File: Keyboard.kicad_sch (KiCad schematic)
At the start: 39 parts, among them J1 USB_C_Receptacle, J2 Conn_02x01, J4 FFC2B35-16-G_REVA2, Q1 PMOS, Q2 NMOS, Q3 NMOS, U1 VBUS54CV-HSF-G4-08, U3 MCP73831-2-OT, U4 LM1117DT-3.3, U5 ESP32-S3-WROOM-1-N16R2

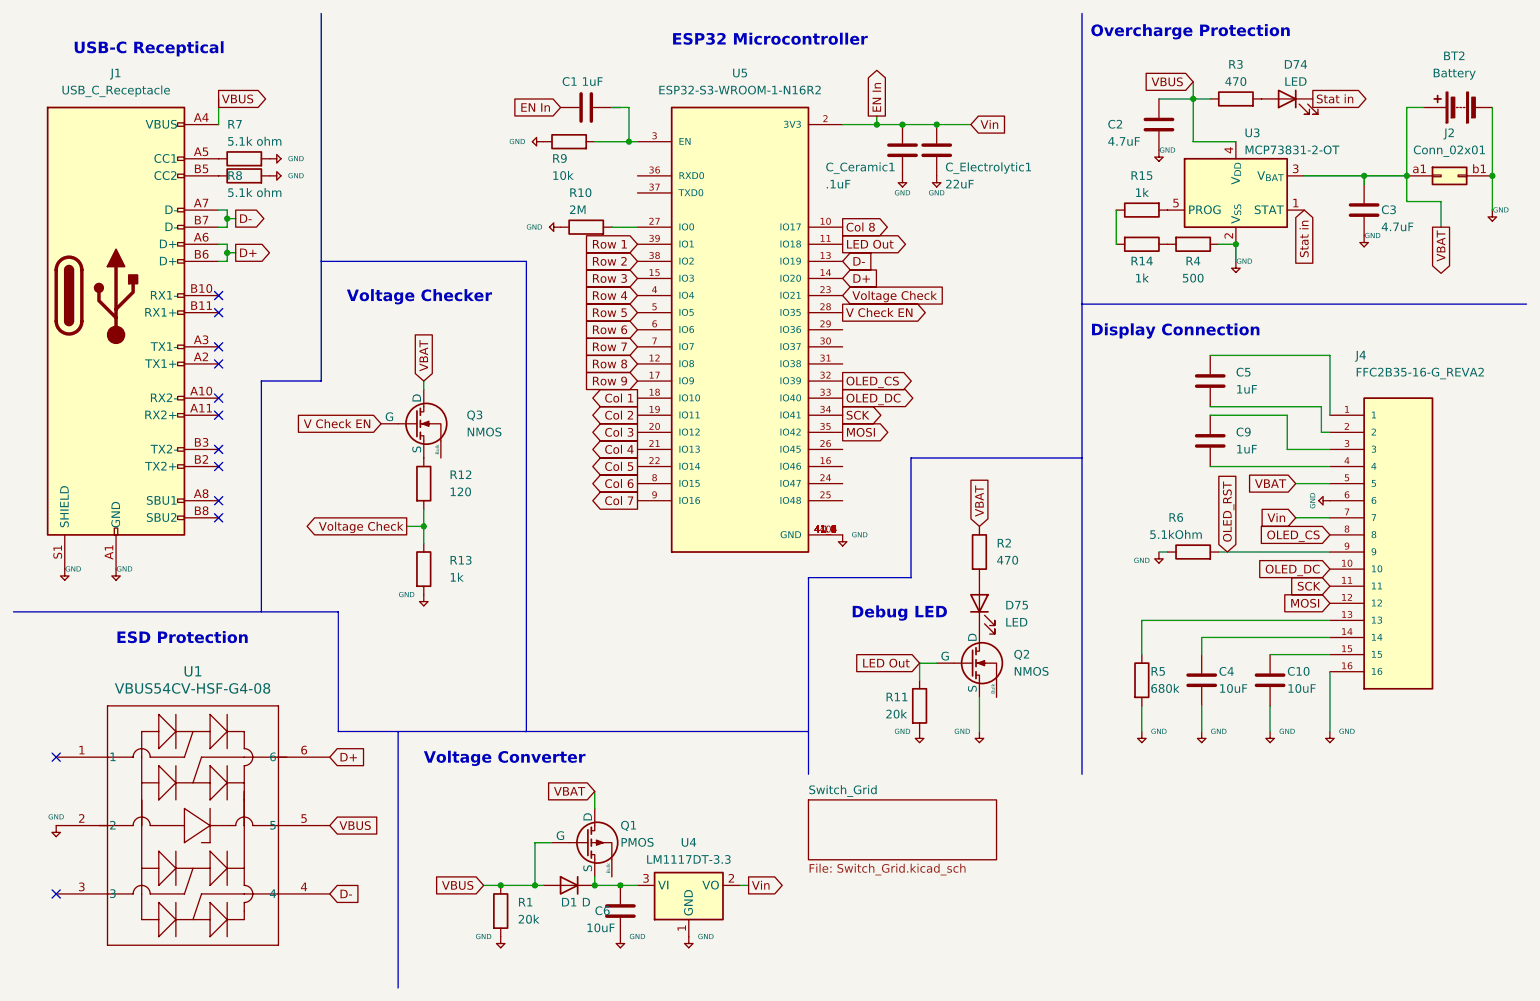
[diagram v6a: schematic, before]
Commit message: finished logic layout, need to connect pins to keys
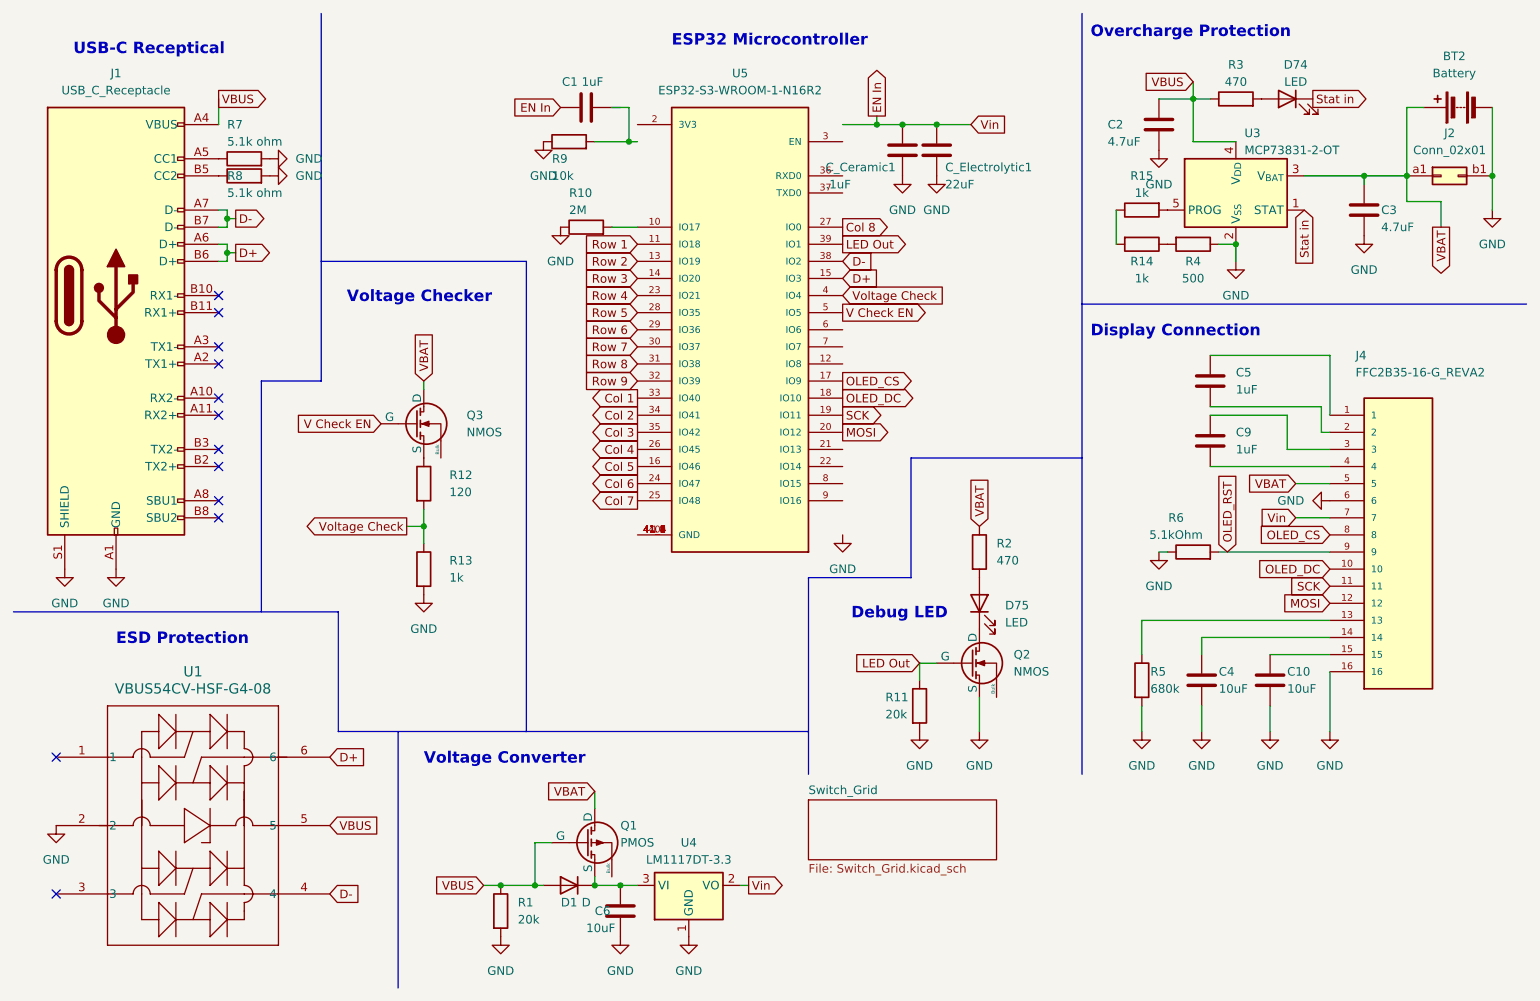
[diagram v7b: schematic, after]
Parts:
- J1: footprint Connector_USB:USB_C_Receptacle_Amphenol_12401548E4-2A -> Connector_USB:USB_C_Receptacle_G-Switch_GT-USB-7010ASV
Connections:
- net Col 1: now also U5.33 (IO40); no longer U5.18 (IO10)
- net Col 2: now also U5.34 (IO41); no longer U5.19 (IO11)
- net Col 3: now also U5.35 (IO42); no longer U5.20 (IO12)
- net Col 4: now also U5.26 (IO45); no longer U5.21 (IO13)
- net Col 5: now also U5.16 (IO46); no longer U5.22 (IO14)
- net Col 6: now also U5.24 (IO47); no longer U5.8 (IO15)
- net Col 7: now also U5.25 (IO48); no longer U5.9 (IO16)
- net Col 8: now also U5.27 (IO0); no longer U5.10 (IO17)
- net D+: now also U5.15 (IO3); no longer U5.14 (IO20)
- net D-: now also U5.38 (IO2); no longer U5.13 (IO19)
- net EN In: no longer U5.2 (3V3)
- net LED Out: now also U5.39 (IO1); no longer U5.11 (IO18)
- net MOSI: now also U5.20 (IO12); no longer U5.35 (IO42)
- net OLED_CS: now also U5.17 (IO9); no longer U5.32 (IO39)
- net OLED_DC: now also U5.18 (IO10); no longer U5.33 (IO40)
- net Row 1: now also U5.11 (IO18); no longer U5.39 (IO1)
- net Row 2: now also U5.13 (IO19); no longer U5.38 (IO2)
- net Row 3: now also U5.14 (IO20); no longer U5.15 (IO3)
- net Row 4: now also U5.23 (IO21); no longer U5.4 (IO4)
- net Row 5: now also U5.28 (IO35); no longer U5.5 (IO5)
- net Row 6: now also U5.29 (IO36); no longer U5.6 (IO6)
- net Row 7: now also U5.30 (IO37); no longer U5.7 (IO7)
- net Row 8: now also U5.31 (IO38); no longer U5.12 (IO8)
- net Row 9: now also U5.32 (IO39); no longer U5.17 (IO9)
- net SCK: now also U5.19 (IO11); no longer U5.34 (IO41)
- net V Check EN: now also U5.5 (IO5); no longer U5.28 (IO35)
- net Voltage Check: now also U5.4 (IO4); no longer U5.23 (IO21)
- net at R10.2: now also U5.10 (IO17); no longer U5.27 (IO0)
- net at C1.2, R9.2: no longer U5.3 (EN)
- net +5V renamed GND
- net GND: no longer U5.1 (GND), U5.40 (GND), U5.41_1 (GND), U5.41_2 (GND), U5.41_3 (GND), U5.41_4 (GND), U5.41_5 (GND), U5.41_6 (GND), U5.41_7 (GND), U5.41_8 (GND), U5.41_9 (GND)
- new net: U5.1 (GND), U5.40 (GND), U5.41_1 (GND), U5.41_2 (GND), U5.41_3 (GND), U5.41_4 (GND), U5.41_5 (GND), U5.41_6 (GND), U5.41_7 (GND), U5.41_8 (GND), U5.41_9 (GND)

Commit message: made further progress on the keyboard pcb
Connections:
- net Col 1: now also U5.18 (IO10); no longer U5.33 (IO40)
- net Col 2: now also U5.19 (IO11); no longer U5.34 (IO41)
- net Col 3: now also U5.20 (IO12); no longer U5.35 (IO42)
- net Col 4: now also U5.22 (IO14); no longer U5.26 (IO45)
- net Col 5: now also U5.21 (IO13); no longer U5.16 (IO46)
- net Col 6: now also U5.8 (IO15); no longer U5.24 (IO47)
- net Col 7: now also U5.9 (IO16); no longer U5.25 (IO48)
- net Col 8: now also U5.10 (IO17); no longer U5.27 (IO0)
- net D+: now also U5.14 (IO20); no longer U5.15 (IO3)
- net D-: now also U5.13 (IO19); no longer U5.38 (IO2)
- net EN In: now also U5.2 (3V3)
- net GND: now also U5.1 (GND), U5.40 (GND), U5.41_1 (GND), U5.41_2 (GND), U5.41_3 (GND), U5.41_4 (GND), U5.41_5 (GND), U5.41_6 (GND), U5.41_7 (GND), U5.41_8 (GND), U5.41_9 (GND)
- net LED Out: now also U5.11 (IO18); no longer U5.39 (IO1)
- net MOSI: now also U5.35 (IO42); no longer U5.20 (IO12)
- net OLED_CS: now also U5.32 (IO39); no longer U5.17 (IO9)
- net OLED_DC: now also U5.33 (IO40); no longer U5.18 (IO10)
- net Row 1: now also U5.39 (IO1); no longer U5.11 (IO18)
- net Row 2: now also U5.38 (IO2); no longer U5.13 (IO19)
- net Row 3: now also U5.15 (IO3); no longer U5.14 (IO20)
- net Row 4: now also U5.4 (IO4); no longer U5.23 (IO21)
- net Row 5: now also U5.5 (IO5); no longer U5.28 (IO35)
- net Row 6: now also U5.6 (IO6); no longer U5.29 (IO36)
- net Row 7: now also U5.7 (IO7); no longer U5.30 (IO37)
- net Row 8: now also U5.12 (IO8); no longer U5.31 (IO38)
- net Row 9: now also U5.17 (IO9); no longer U5.32 (IO39)
- net SCK: now also U5.34 (IO41); no longer U5.19 (IO11)
- net V Check EN: now also U5.28 (IO35); no longer U5.5 (IO5)
- net Voltage Check: now also U5.23 (IO21); no longer U5.4 (IO4)
- net at R10.2: now also U5.27 (IO0); no longer U5.10 (IO17)
- net at U5.3 (EN): now also C1.2, R9.2
